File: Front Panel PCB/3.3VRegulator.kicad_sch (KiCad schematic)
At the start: 2 parts, among them J2 Main Power In, J8 Power To Amp

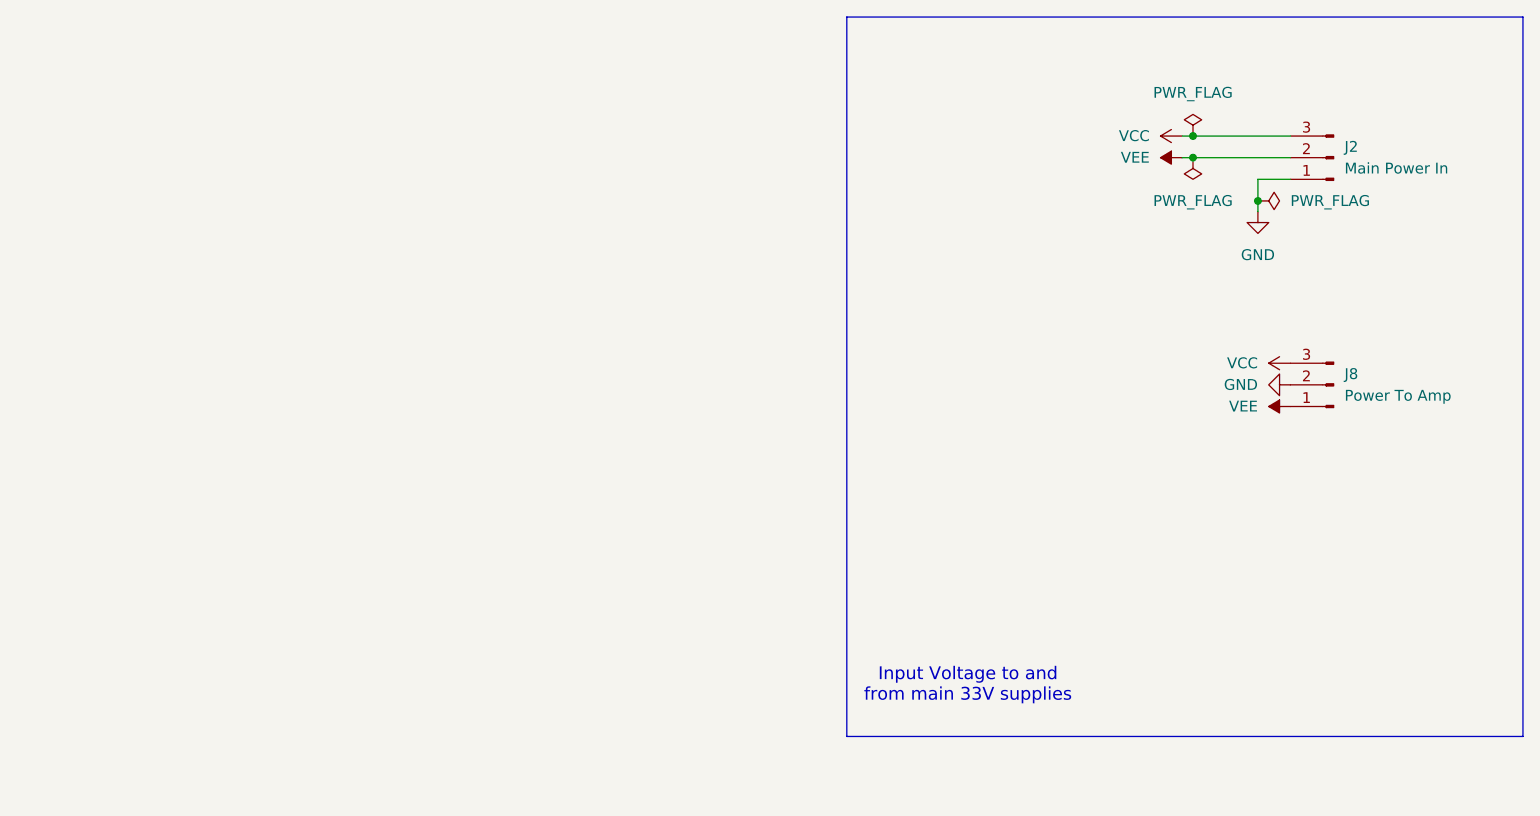
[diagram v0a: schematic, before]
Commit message: Hierarichal sheets and started PCB design
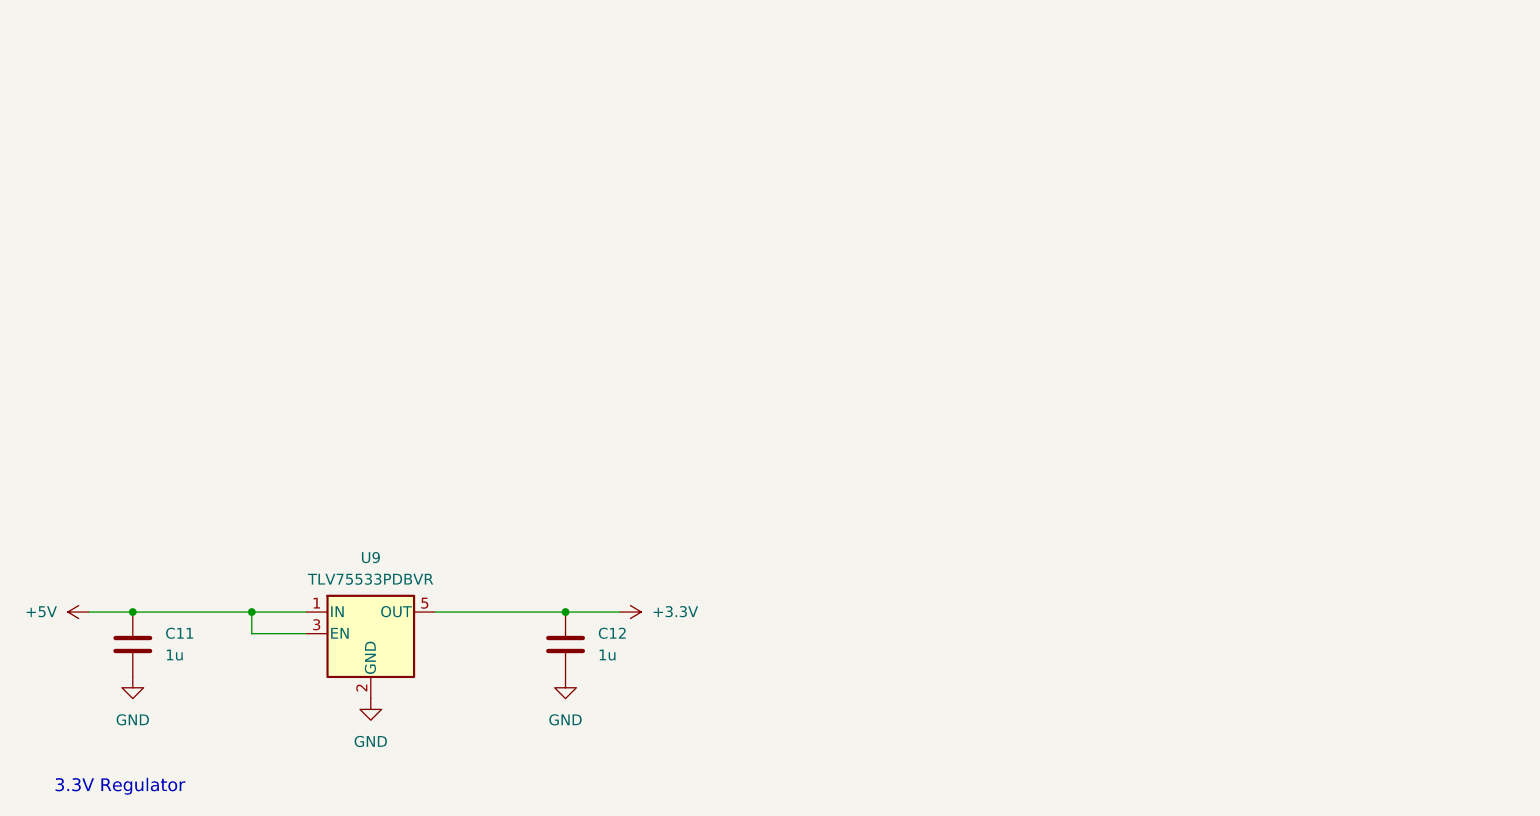
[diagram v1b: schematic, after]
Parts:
- removed J2: Main Power In, 1829167:PHOENIX_1829167, symbol Connector:Conn_01x03_Pin
- removed J8: Power To Amp, 1829167:PHOENIX_1829167, symbol Connector:Conn_01x03_Pin
- added C11, C12: 1u, GJ821BR71H105KA12L:CAPC2012X135N, symbol Device:C
- added U9: TLV75533PDBVR, Package_TO_SOT_SMD:SOT-23-5, symbol Regulator_Linear:TLV75533PDBV
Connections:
- net GND: now also C11.2, C12.2, U9.2 (GND)
- new net +3.3V: C12.1, U9.5 (OUT)
- new net +5V: C11.1, U9.1 (IN), U9.3 (EN)
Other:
- note added: "3.3V Regulator"
- note removed: "Input Voltage to and from main 33V supplies"
- company: University of Stellenbosch -> (none)
- title: Power Supplies -> (none)
